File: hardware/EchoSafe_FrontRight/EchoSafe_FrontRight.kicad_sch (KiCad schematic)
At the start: 5 parts, among them J1 Conn_Harness_09, M2 C0720B001F

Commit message: Assign footprints across all 5 projects, add missing fp-lib-table
Target confirmed as a compact near-final wearable, not an early bring-up
prototype -- choices below favor small/soldered over socketed/header.

Fixed a regression: splitting into 5 projects had wiped the mic
(LGA_CAV_IVS) and motor (C0720B001F:XDCR_C0720B001F) footprints that
already existed pre-split -- the instance generator zeroed every new
component's footprint unconditionally. Restored both from the pre-split
commit.

Fixed a second, pre-existing bug: no fp-lib-table ever existed in any
version of this project (same class of gap as the sym-lib-table issue
found earlier this session), and three footprint references
(LGA_CAV_IVS, ESP32-S3-WROOM-1_EXP, 21-0136I_T1633-4_MXM) were bare
names with no library prefix -- neither would have resolved in KiCad's
PCB editor even with a table present. Created fp-lib-table in the
central pod (ESP32-S3-WROOM-1, MAX98357AETE-T) and all 4 module projects
(ICS-43434, C0720B001F), then added the missing prefixes. Verified every
path resolves to a real .kicad_mod file on disk.

Newly assigned:
- All 17 capacitors -> Capacitor_SMD:C_0603_1608Metric
- BT1 (battery) -> Connector_JST:JST_PH_S2B_PH_K_1x02_P2.00mm_Horizontal
  (confirmed: this battery ships with a pre-attached JST-PH connector)
- LD1 (LD1117V33) -> 3-pin 2.54mm header pattern (matches the real
  breakout's hole spacing regardless of pins-vs-wire assembly)
- J1/central pod (TP4056) -> 4-pin 2.54mm header pattern (placeholder --
  flagged to verify against the actual purchased board's hole spacing)
- J2-J5 (pod) + each module's J1 -> JST-SH 1.0mm pitch, 9-pin or 7-pin
  (compact-wearable target ruled out bulkier 2.54mm headers for a
  7-9-conductor cable through the headband)

Left unassigned: LS1/LS2 (speakers) -- no specific part chosen yet,
capsule dimensions vary too much to guess a meaningful footprint.

Verified across all 5 files independently: paren balance intact, no
duplicate UUIDs, no duplicate re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
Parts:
- C10: footprint (none) -> Capacitor_SMD:C_0603_1608Metric
- J1: footprint (none) -> Connector_JST:JST_SH_BM09B-SRSS-TB_1x09-1MP_P1.00mm_Horizontal
- M2: footprint (none) -> C0720B001F:XDCR_C0720B001F
- MIC2: footprint (none) -> ICS-43434:LGA_CAV_IVS
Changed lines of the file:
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@@
 			(effects (font (size 1.27 1.27)) (justify left))
 		)
-		(property "Footprint" ""
+		(property "Footprint" "ICS-43434:LGA_CAV_IVS"
 			(at 50 50 0)
 			(effects (font (size 1.27 1.27) (italic yes)) (hide yes))
@@
 			(effects (font (size 1.27 1.27)) (justify left))
 		)
-		(property "Footprint" ""
+		(property "Footprint" "Capacitor_SMD:C_0603_1608Metric"
 			(at 30 50 0)
 			(effects (font (size 1.27 1.27) (italic yes)) (hide yes))
@@
 			(effects (font (size 1.27 1.27)) (justify left))
 		)
-		(property "Footprint" ""
+		(property "Footprint" "C0720B001F:XDCR_C0720B001F"
 			(at 50 90 0)
 			(effects (font (size 1.27 1.27) (italic yes)) (hide yes))
@@
 			(effects (font (size 1.27 1.27)) (justify left))
 		)
-		(property "Footprint" ""
+		(property "Footprint" "Connector_JST:JST_SH_BM09B-SRSS-TB_1x09-1MP_P1.00mm_Horizontal"
 			(at 120 50 0)
 			(effects (font (size 1.27 1.27) (italic yes)) (hide yes))

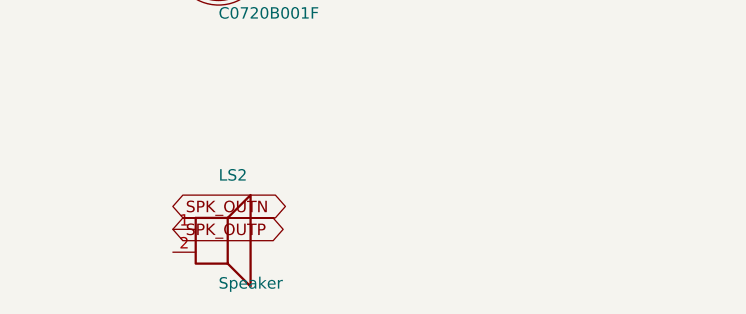
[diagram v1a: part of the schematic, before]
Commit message: Assign speaker (LS1/LS2) footprint from real part number
DigiKey 1528-4227-ND = Adafruit #4227 "Mini Oval Speaker," 8 ohm, 1W,
30x20x5mm -- verified via DigiKey/Adafruit's own product listings, not
from memory (same standard as the TCA9548A datasheet lookup earlier this
session).

Notable finding that changed the footprint choice: this part connects
via a Molex PicoBlade 1.25mm-pitch 2-pin connector on a ~10mm cable, not
bare wire leads -- a generic "speaker footprint" assumption would have
been wrong. Set Footprint to
Connector_Molex:Molex_PicoBlade_53261-0271_1x02-1MP_P1.25mm_Horizontal,
confirmed against KiCad's own official footprint library source (unlike
the JST-SH harness connector names chosen last session, which are
best-effort without a live KiCad install to check against).

Also worth noting: Adafruit's own product page recommends this exact
speaker for use with MAX98357A, which is what this design already uses --
independent confirmation the part fits.

All footprints across all 5 hardware projects are now assigned.

Co-Authored-By: Claude Sonnet 5 <noreply@anthropic.com>
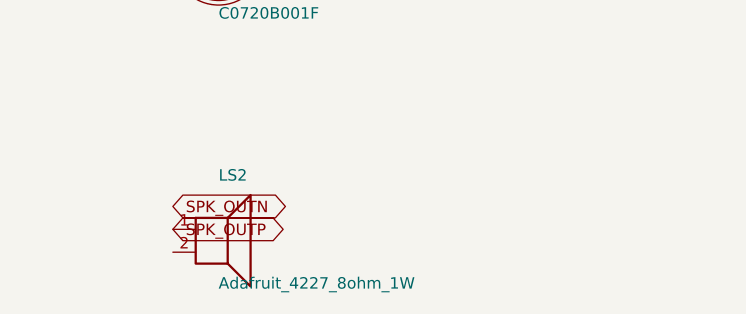
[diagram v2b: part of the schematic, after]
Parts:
- LS2: value Speaker -> Adafruit_4227_8ohm_1W; footprint (none) -> Connector_Molex:Molex_PicoBlade_53261-0271_1x02-1MP_P1.25mm_Horizontal
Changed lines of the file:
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@@
 			(effects (font (size 1.27 1.27)) (justify left))
 		)
-		(property "Value" "Speaker"
+		(property "Value" "Adafruit_4227_8ohm_1W"
 			(at 50 126 0)
 			(effects (font (size 1.27 1.27)) (justify left))
 		)
-		(property "Footprint" ""
+		(property "Footprint" "Connector_Molex:Molex_PicoBlade_53261-0271_1x02-1MP_P1.25mm_Horizontal"
 			(at 50 120 0)
 			(effects (font (size 1.27 1.27) (italic yes)) (hide yes))
 		)
+		(property "Datasheet" "https://cdn-shop.adafruit.com/product-files/4227/4227_datasheet.pdf"
+			(at 50 120 0)
+			(effects (font (size 1.27 1.27)) (hide yes))
+		)
+		(property "Description" "Adafruit #4227 / DigiKey 1528-4227-ND -- Mini Oval Speaker, 8 ohm 1W, 30x20x5mm, Molex PicoBlade 1.25mm 2-pin connector on ~10mm cable"
+			(at 50 120 0)
+			(effects (font (size 1.27 1.27)) (hide yes))
+		)
 		(pin "1"

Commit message: Fix JST-SH footprint naming error, verify TP4056 pin spacing
Resolved both gaps flagged at the end of the footprint pass:

- JST-SH harness connector names were an unverified guess using a
  "BM0xB-SRSS-TB" prefix. Fetched the actual files from KiCad's own
  kicad-footprints repo and confirmed the real prefix is "SM0xB-SRSS-TB"
  -- JST_SH_SM09B-SRSS-TB_1x09-1MP_P1.00mm_Horizontal (9 signal + 2
  mounting pads) and JST_SH_SM07B-SRSS-TB_1x07-1MP_P1.00mm_Horizontal
  (7 signal + 2 mounting pads) both verified to exist with correct pad
  counts. Fixed all 8 occurrences across all 5 projects (J2/J3/J4/J5 in
  the central pod, one J1 per module).

- Checked TP4056 module pin spacing against multiple independent
  sources; 2.54mm/0.1" through-hole pitch is standard across common
  module variants, confirming the PinHeader_1x04_P2.54mm_Vertical
  placeholder already assigned. Noted this should still get a quick
  physical check against the actual board, since "HiLetGo TP4056"
  covers slightly different revisions.

Verified across all 5 files: paren balance intact, unique UUIDs.

Co-Authored-By: Claude Sonnet 5 <noreply@anthropic.com>
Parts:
- J1: footprint Connector_JST:JST_SH_BM09B-SRSS-TB_1x09-1MP_P1.00mm_Horizontal -> Connector_JST:JST_SH_SM09B-SRSS-TB_1x09-1MP_P1.00mm_Horizontal
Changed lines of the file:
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@@
 			(effects (font (size 1.27 1.27)) (justify left))
 		)
-		(property "Footprint" "Connector_JST:JST_SH_BM09B-SRSS-TB_1x09-1MP_P1.00mm_Horizontal"
+		(property "Footprint" "Connector_JST:JST_SH_SM09B-SRSS-TB_1x09-1MP_P1.00mm_Horizontal"
 			(at 120 50 0)
 			(effects (font (size 1.27 1.27) (italic yes)) (hide yes))

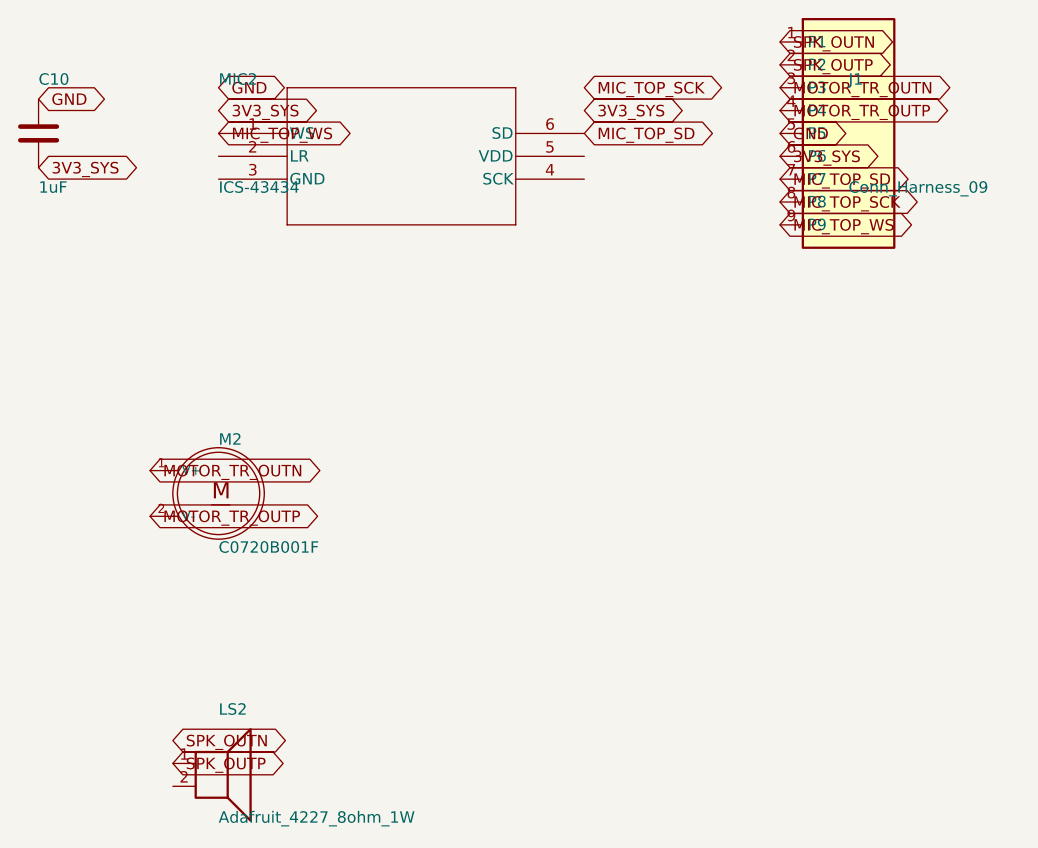
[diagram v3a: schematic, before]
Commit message: Fix session-wide Y-axis coordinate bug, power the ESP32 module
Discovered KiCad is actually installed on this machine and ran real
kicad-cli sch erc against every schematic for the first time, instead of
continuing to rely on text-based invariant checks alone. This surfaced a
fundamental bug affecting every schematic edit made this session:

Every label/wire/no-connect placed with a nonzero local Y pin offset used
placement_y + local_y instead of the correct placement_y - local_y --
KiCad symbol graphics are authored Y-up, the sheet is Y-down, and that
flip applies even at angle=0/no-mirror. The two formulas only agree when
local_y=0, which is why isolated spot-checks earlier in the session
happened to look right.

Fixed via a from-scratch single-pass correction (not sequential in-place
edits -- an earlier attempt at that approach introduced a second bug,
caught before committing: correcting one label could make its new
position collide with a not-yet-corrected label's old position, causing
a later step to move the wrong element). Final approach computes every
correction from an unmodified snapshot and applies them all in one pass
from a fixed baseline.

Verified by ERC before/after, not by the tooling that produced the bug:
- All 4 module projects: 21/21/17/17 raw violations -> 9/9/8/8, all
  expected (spare GPIOs, the already-documented placeholder-connector
  warning, and cross-project "power not driven" since the driving
  component lives in a different project's file).
- Central pod: down to 0 dangling labels, 0 genuinely unconnected pins.
  Remaining ~200 ERC items are exclusively pairwise power-rail type-
  mismatch warnings (expected on any board with this many ICs sharing
  3V3_SYS/GND), cosmetic off-grid warnings, and spare pins.

Also fixed, a genuine gap this same ERC pass surfaced (unrelated to the
Y-axis bug): the ESP32 module's own 3V3/GND/EN pins were never wired to
anything -- every peripheral got connected this session, the MCU's own
supply pins we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
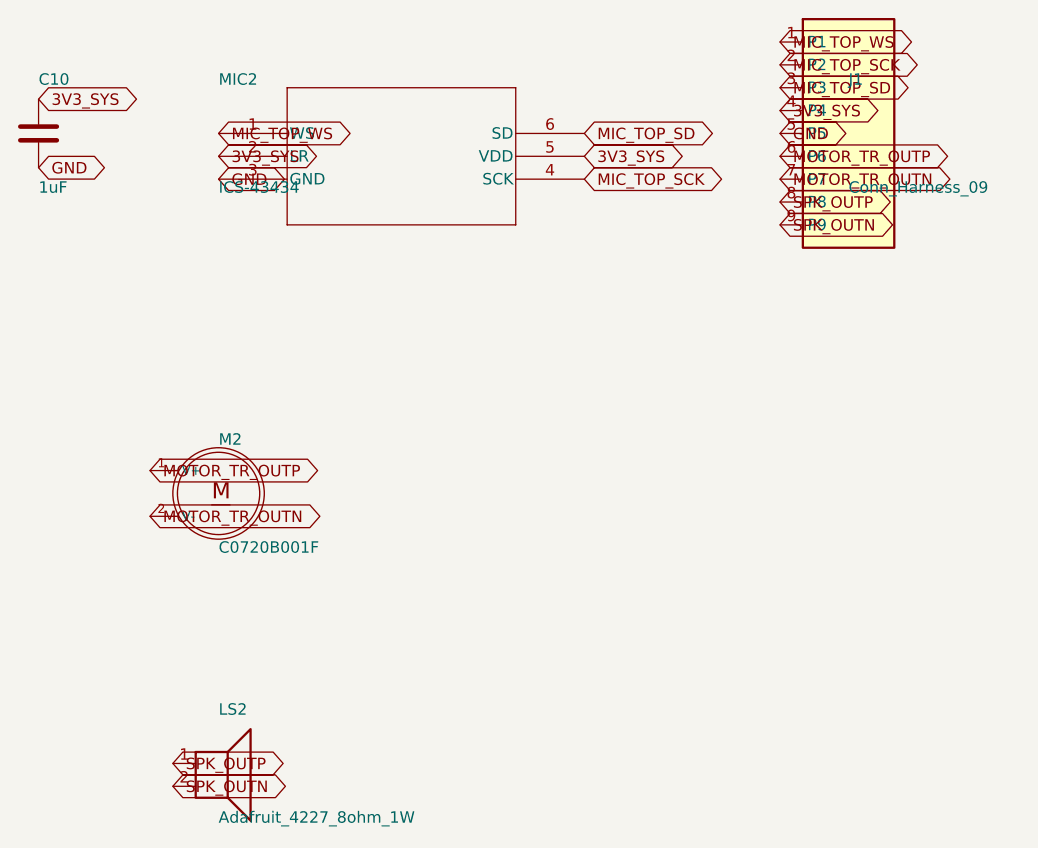
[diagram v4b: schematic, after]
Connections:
- net 3V3_SYS: now also C10.1, J1.4 (P4), MIC2.2 (LR), MIC2.5 (VDD); no longer C10.2, J1.6 (P6)
- net GND: now also C10.2, MIC2.3 (GND); no longer C10.1
- net MIC_TOP_SCK: now also J1.2 (P2), MIC2.4 (SCK); no longer J1.8 (P8)
- net MIC_TOP_SD: now also J1.3 (P3); no longer J1.7 (P7)
- net MIC_TOP_WS: now also J1.1 (P1); no longer J1.9 (P9)
- net MOTOR_TR_OUTN: now also J1.7 (P7), M2.2 (V-); no longer J1.3 (P3), M2.1 (V+)
- net MOTOR_TR_OUTP: now also J1.6 (P6), M2.1 (V+); no longer J1.4 (P4), M2.2 (V-)
- net SPK_OUTN: now also J1.9 (P9), LS2.2; no longer J1.1 (P1)
- net SPK_OUTP: now also J1.8 (P8); no longer J1.2 (P2)

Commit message: Replace mic footprint with one authored from the real datasheet
Discovered while starting PCB placement: the original SnapEDA-imported
LGA_CAV_IVS.kicad_mod (pre-dates this session) doesn't match the real
ICS-43434 part. Its GND pad (3) is a tiny 0.127x0.127mm corner pad, and
a non-electrical mechanical hole occupies pad number "6", pushing the
real 6th electrical pad to "7" -- one off from the schematic symbol's
pin 6 (SD).

Fetched and read InvenSense's actual datasheet (DS-000069 Rev 1.0) to
verify: GND is really a large ring pad (1.025mm inner / 1.625mm outer
diameter) surrounding the microphone's acoustic port -- nothing like
what the footprint had.

Authored a replacement footprint (ICS-43434_LGA6, new library
Mics_Corrected.pretty) using KiCad's own pcbnew Python API directly from
the datasheet's Figure 3 (pin positions) and Figure 13 (land pattern
dimensions): 5 roundrect signal pads at the datasheet's stated 0.6x0.9mm
size / 0.9mm pitch, GND simplified to a solid circular pad at the ring's
outer diameter (electrically equivalent, though it omits the board-level
acoustic port hole the datasheet also specifies -- that's a PCB-outline
feature, not something a footprint file can express, and is flagged in
CLAUDE.md as a manual step for actual layout).

Round-trip verified by reloading the saved file through
pcbnew.FootprintLoad() and checking pad count/positions/shapes. Updated
fp-lib-table in all 4 module projects and MIC1-4's Footprint property.
Re-ran ERC afterward -- unchanged (9/9/8/8), confirming this was purely
a physical/PCB-level fix with no schematic-connectivity impact.

Co-Authored-By: Claude Sonnet 5 <noreply@anthropic.com>
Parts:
- MIC2: footprint ICS-43434:LGA_CAV_IVS -> ICS-43434:ICS-43434_LGA6
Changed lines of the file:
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@@
 			(effects (font (size 1.27 1.27)) (justify left))
 		)
-		(property "Footprint" "ICS-43434:LGA_CAV_IVS"
+		(property "Footprint" "ICS-43434:ICS-43434_LGA6"
 			(at 50 50 0)
 			(effects (font (size 1.27 1.27) (italic yes)) (hide yes))

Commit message: Generate fab outputs (gerbers, drill, CPL, BOM) for all 5 boards
kicad-cli pcb export gerbers/drill/pos and sch export bom, into each
project's own outputs/ folder, zipped for direct fab upload. Standard
2-layer gerber set (confirmed 2-layer by checking the layer table, not
assumed); drill files split PTH/NPTH since the mic modules have a real
NPTH hole (H1, the acoustic port) -- spot-checked the NPTH file directly
to confirm it's really in there.

Generating the BOM surfaced a real gap: J2/J3/J4/J5 (central pod), J1
(all 4 modules), and LS1 (front modules) still had their schematic
Footprint field pointing at the stock Connector_JST/Connector_Molex
footprint, not the Connectors_PinMarked override from the last commit --
because that fix only touched footprint instances already placed on the
PCB, never the originating schematic symbols. Left alone, a future
"Update PCB from Schematic" would have silently reverted the pin-marker
fix. Fixed by updating the Footprint property in each .kicad_sch;
confirmed via kicad-cli sch erc that violation counts on all 5 schematics
are unchanged (metadata-only edit, no electrical effect).

All 5 boards reconfirmed at 0 DRC violations, full severity.

Co-Authored-By: Claude Sonnet 5 <noreply@anthropic.com>
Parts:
- J1: footprint Connector_JST:JST_SH_SM09B-SRSS-TB_1x09-1MP_P1.00mm_Horizontal -> Connectors_PinMarked:JST_SH_SM09B-SRSS-TB_1x09-1MP_P1.00mm_Horizontal
- LS2: footprint Connector_Molex:Molex_PicoBlade_53261-0271_1x02-1MP_P1.25mm_Horizontal -> Connectors_PinMarked:Molex_PicoBlade_53261-0271_1x02-1MP_P1.25mm_Horizontal
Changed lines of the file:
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@@
 			(effects (font (size 1.27 1.27)) (justify left))
 		)
-		(property "Footprint" "Connector_Molex:Molex_PicoBlade_53261-0271_1x02-1MP_P1.25mm_Horizontal"
+		(property "Footprint" "Connectors_PinMarked:Molex_PicoBlade_53261-0271_1x02-1MP_P1.25mm_Horizontal"
 			(at 50 120 0)
 			(effects (font (size 1.27 1.27) (italic yes)) (hide yes))
@@
 			(effects (font (size 1.27 1.27)) (justify left))
 		)
-		(property "Footprint" "Connector_JST:JST_SH_SM09B-SRSS-TB_1x09-1MP_P1.00mm_Horizontal"
+		(property "Footprint" "Connectors_PinMarked:JST_SH_SM09B-SRSS-TB_1x09-1MP_P1.00mm_Horizontal"
 			(at 120 50 0)
 			(effects (font (size 1.27 1.27) (italic yes)) (hide yes))
